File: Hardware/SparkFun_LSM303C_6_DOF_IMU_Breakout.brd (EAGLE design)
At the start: 23.9 x 25.4 mm, 24 parts, among them U1 LSM303C, U2 LM3880

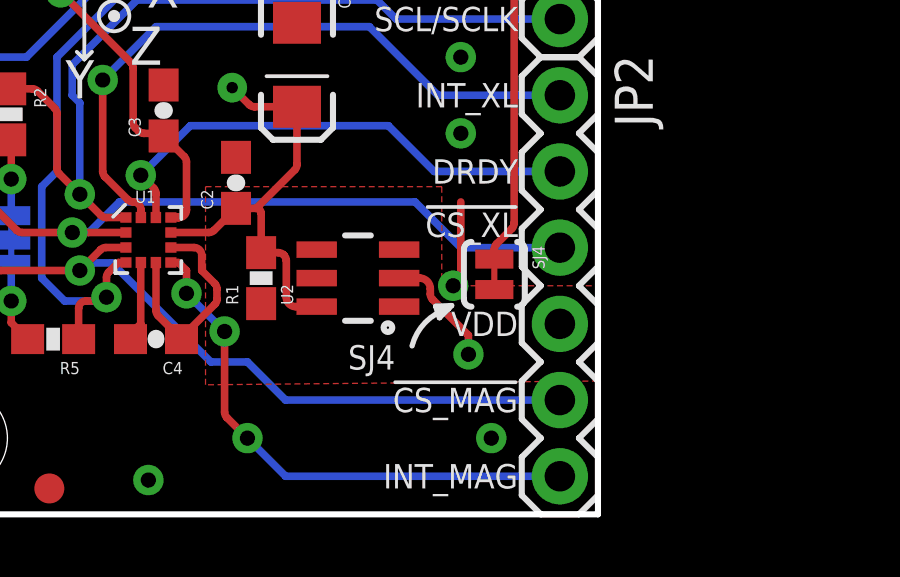
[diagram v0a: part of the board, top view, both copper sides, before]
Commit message: Renamed SJ4 & moved a dim to layer 47
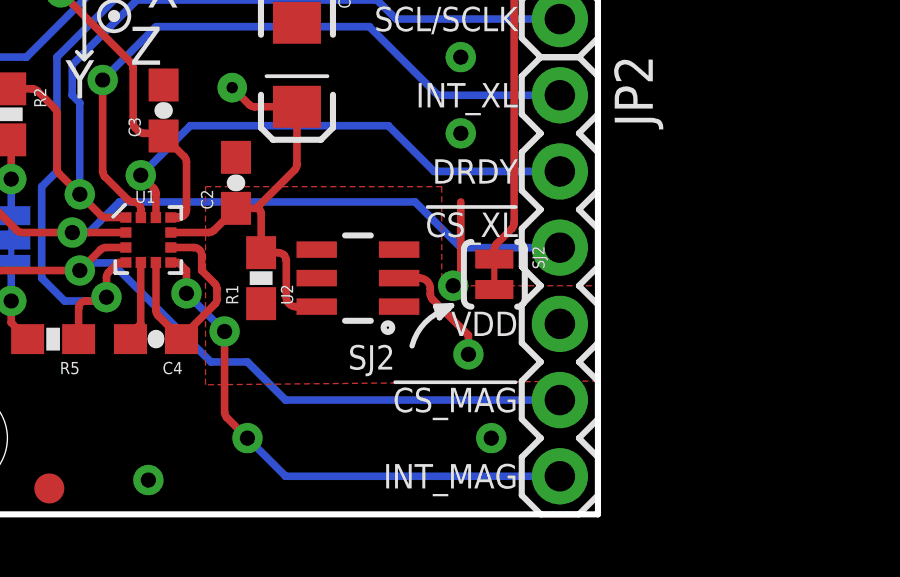
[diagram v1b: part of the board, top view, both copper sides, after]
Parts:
- renumbered SJ4 to SJ2
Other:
- board text added: "SJ2"
- board text removed: "SJ4"
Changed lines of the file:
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@@
 <?xml version="1.0" encoding="utf-8"?>
 <!DOCTYPE eagle SYSTEM "eagle.dtd">
-<eagle version="7.2.0">
+<eagle version="7.3.2">
 <drawing>
 <settings>
@@
 <wire x1="18.5928" y1="6.5532" x2="18.4658" y2="6.9342" width="0.1778" layer="21"/>
 <wire x1="18.4658" y1="6.9342" x2="18.9992" y2="6.9596" width="0.1778" layer="21"/>
-<text x="15.5448" y="5.2324" size="0.8128" layer="21" ratio="15" align="center-left">SJ4</text>
+<text x="15.5448" y="5.2324" size="0.8128" layer="21" ratio="15" align="center-left">SJ2</text>
 <dimension x1="25.4" y1="0" x2="25.4" y2="25.4" x3="28.6004" y3="12.7" textsize="1.778" textratio="15" layer="47" unit="inch"/>
 <dimension x1="2.54" y1="22.86" x2="0" y2="22.86" x3="1.27" y3="27.94" textsize="1.778" textratio="15" layer="47" unit="inch"/>
@@
 <text x="7.5184" y="24.0284" size="0.889" layer="16" font="vector" ratio="20" rot="MR0">&gt;VERSION</text>
 <text x="3.1242" y="9.652" size="0.8128" layer="22" ratio="15" rot="MR0" align="center-left">I2C</text>
-<dimension x1="0" y1="0" x2="23.876" y2="0" x3="11.938" y3="-3.556" textsize="1.778" textratio="15" layer="20" unit="inch"/>
+<dimension x1="0" y1="0" x2="23.876" y2="0" x3="11.938" y3="-3.556" textsize="1.778" textratio="15" layer="47" unit="inch"/>
 <text x="8.382" y="-14.224" size="1.778" layer="51">&gt;DESIGNER</text>
 <text x="12.192" y="27.686" size="1.778" layer="20" font="vector" ratio="15">All units in inches</text>
@@
 <element name="JP1" library="SparkFun-Connectors" package="1X04" value="" x="22.606" y="24.13" rot="R270"/>
 <element name="SJ1" library="SparkFun-Passives" package="PAD-JUMPER-3-3OF3_NC_BY_TRACE_YES_SILK_FULL_BOX" value="" x="4.318" y="9.144" rot="MR90"/>
-<element name="SJ4" library="SparkFun-Passives" package="PAD-JUMPER-2-NC_BY_TRACE_YES_SILK" value="JUMPER-PAD-2-NC_BY_TRACE" x="20.4216" y="8.001" rot="R270"/>
+<element name="SJ2" library="SparkFun-Passives" package="PAD-JUMPER-2-NC_BY_TRACE_YES_SILK" value="JUMPER-PAD-2-NC_BY_TRACE" x="20.4216" y="8.001" rot="R270"/>
 <element name="TP1" library="SparkFun-Passives" package="TP_15TH" value="VDD_TP" x="11.684" y="14.224"/>
 <element name="STANDOFF1" library="SparkFun-Electromechanical" package="STAND-OFF" value="STAND-OFF" x="2.54" y="22.86"/>
@@
 <contactref element="U2" pad="1"/>
 <contactref element="JP2" pad="4"/>
-<contactref element="SJ4" pad="2"/>
+<contactref element="SJ2" pad="2"/>
 <polygon width="0.254" layer="1">
 <vertex x="23.876" y="7.62"/>
@@
 <contactref element="SJ1" pad="2"/>
 <contactref element="JP1" pad="2"/>
-<contactref element="SJ4" pad="1"/>
+<contactref element="SJ2" pad="1"/>
 <wire x1="9.64" y1="9.894" x2="9.652" y2="9.906" width="0.254" layer="1"/>
 <wire x1="9.652" y1="9.906" x2="9.906" y2="9.906" width="0.254" layer="1"/>
